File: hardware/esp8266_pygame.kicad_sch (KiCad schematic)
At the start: 27 parts, among them J1 Conn_01x12, J2 Conn_01x12, J3 Conn_01x03, J4 Conn_01x02, J5 Micro_SD_Card, J6 Conn_01x08, Q1 NPN, SW1 SW_Push, SW2 SW_Push, SW3 SW_Push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

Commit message: New PCB schematic ready
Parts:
- removed BZ1: Buzzer, symbol Device:Buzzer
- removed C1: 4u7, symbol Device:C
- removed D1: LED, symbol Device:LED
- removed J1, J2: Conn_01x12, symbol Connector_Generic:Conn_01x12
- removed J3: Conn_01x03, symbol Connector_Generic:Conn_01x03
- removed J4: Conn_01x02, symbol Connector_Generic:Conn_01x02
- removed J5: Micro_SD_Card, symbol Connector:Micro_SD_Card
- removed J6: Conn_01x08, symbol Connector_Generic:Conn_01x08
- removed Q1: NPN, symbol Simulation_SPICE:NPN
- removed R6: 142k, symbol Device:R
- removed R7: 200, symbol Device:R
- removed R8: 10k, symbol Device:R
- removed RN1: 9 x 10k, Resistor_THT:R_Array_SIP10, symbol Device:R_Network09
- removed RV?: 10k, symbol Device:R_Potentiometer
- removed SW1, SW2, SW3, SW4, SW5, SW6, SW7: SW_Push, symbol Switch:SW_Push
- removed SW8: SW_SPST, symbol Switch:SW_SPST
- removed U1: PCF8574, symbol Interface_Expansion:PCF8574
- added J1: Conn_02x02_Odd_Even, symbol Connector_Generic:Conn_02x02_Odd_Even
- added R2: 50k, symbol Device:R
- added R4: 10k, symbol Device:R
- added U1: ESP-07, RF_Module:ESP-07, symbol RF_Module:ESP-07
- R1: value 1k -> 0
- R3: value 100 -> 50k
- R5: value 220k -> 10k
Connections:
- net LED is gone; now on net LCD_CE: R3.1
- net +3.3V: now also R3.2, R5.2, R4.2, U1.8 (VCC)
- net BUZZER: now also R2.2, U1.6 (GPIO12)
- net GND: now also R2.1, U1.9 (GND)
- net LCD_CE: now also J1.4 (Pin_4), U1.12 (GPIO0)
- net LCD_DC: now also U1.11 (GPIO2)
- net LCD_RST: now also R1.2
- net MOSI: now also U1.7 (GPIO13)
- net RXD: now also J1.2 (Pin_2), U1.15 (GPIO3/RXD)
- net SCK: now also U1.5 (GPIO14)
- net SCL: now also U1.14 (GPIO5)
- net SDA: now also U1.13 (GPIO4)
- net TXD: now also J1.1 (Pin_1), U1.16 (GPIO1/TXD)
- net Ubatt: now also U1.2 (ADC); no longer R5.2
- net at R1.1: now also U1.4 (GPIO16)
- net +BATT renamed ~{RST}
- net ~{RST}: now also J1.3 (Pin_3), U1.1 (~{RST})
- new net BACKLIGHT_PWM: U1.10 (GPIO15)
- new net CHIP_EN: R4.1, U1.3 (EN)
- no-connect marks 9 -> 0
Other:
- added sheet Human Machine Interface Section (hmi.kicad_sch)
- added sheet Power section (power_section.kicad_sch)
- note removed: "3V3"
- note removed: "5V"
- note removed: "A0"
- note removed: "Battery"
- note removed: "Board Batt Conn"
- note removed: "CTS"
- note removed: "DTR"
- note removed: "EN"
- note removed: "GND"
- note removed: "GPIO0"
- note removed: "GPIO1"
- note removed: "GPIO12"
- note removed: "GPIO13"
- note removed: "GPIO14"
- note removed: "GPIO15"
- note removed: "GPIO16"
- note removed: "GPIO2"
- note removed: "GPIO3"
- note removed: "GPIO4"
- note removed: "GPIO5"
- note removed: "RST"

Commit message: Second revision of schematic
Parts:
- removed R4: 10k, symbol Device:R
- added R5, R6: 4k7, Resistor_SMD:R_0603_1608Metric, symbol Device:R
- J1: footprint (none) -> Connector_PinHeader_2.54mm:PinHeader_2x02_P2.54mm_Vertical
- R1, R2, R3: footprint (none) -> Resistor_SMD:R_0603_1608Metric
- R4: renamed from R5; footprint (none) -> Resistor_SMD:R_0603_1608Metric
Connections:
- net +3.3V: now also R5.2, R6.2
- net SCL: now also R6.1
- net SDA: now also R5.1
- net CHIP_EN: no longer names the net of U1.3 (EN)
- no-connect marks 0 -> 1
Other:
- sheet Human Machine Interface Section ports: added BACKLIGHT_PWM, BUZZER, LCD_CE, LCD_DC, LCD_RST, MOSI, POWER_EN, SCK, SCL, SDA; removed none
- sheet Power section ports: added POWER_EN, Ubatt; removed none
- moved on the sheet: R4

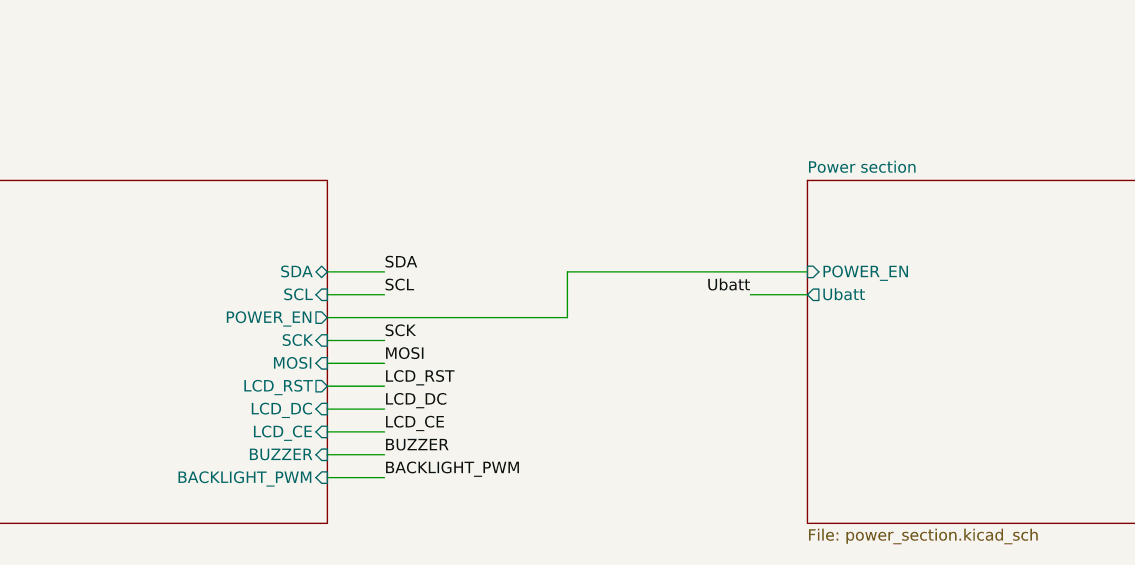
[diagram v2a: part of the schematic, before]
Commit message: Fixed power enable bypass
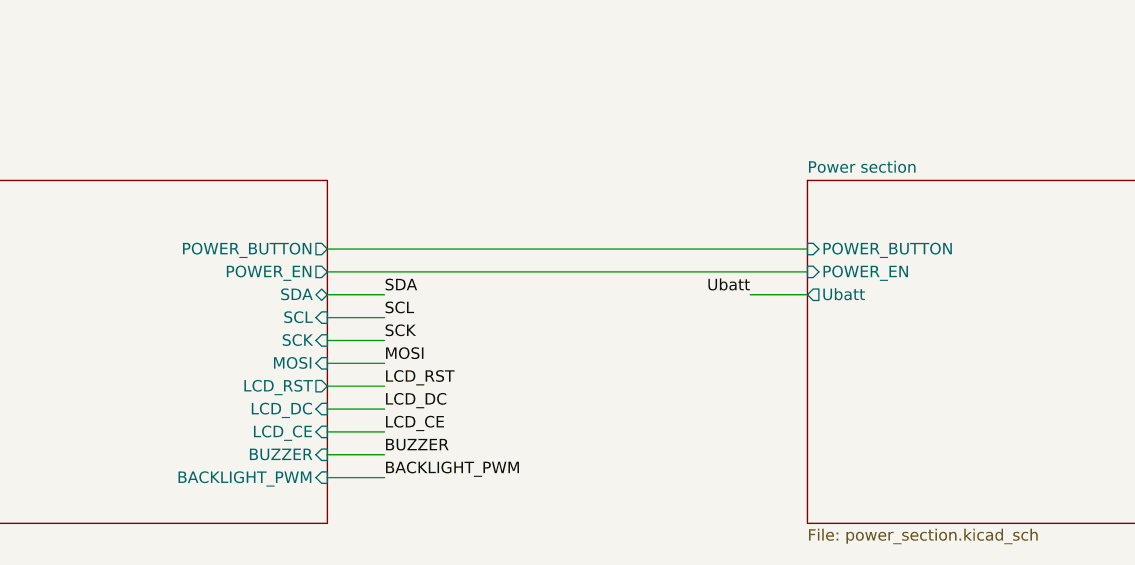
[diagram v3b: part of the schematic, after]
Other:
- sheet Human Machine Interface Section ports: added POWER_BUTTON; removed none
- sheet Power section ports: added POWER_BUTTON; removed none
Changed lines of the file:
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@@
 	(wire
 		(pts
-			(xy 146.05 130.81) (xy 146.05 125.73)
+			(xy 119.38 130.81) (xy 125.73 130.81)
+		)
+		(stroke
+			(width 0)
+			(type default)
+		)
+	)
+	(wire
+		(pts
+			(xy 119.38 123.19) (xy 172.72 123.19)
+		)
+		(stroke
+			(width 0)
+			(type default)
+		)
+	)
+	(wire
+		(pts
+			(xy 85.09 52.07) (xy 93.98 52.07)
+		)
+		(stroke
+			(width 0)
+			(type default)
+		)
+	)
+	(wire
+		(pts
+			(xy 85.09 57.15) (xy 93.98 57.15)
+		)
+		(stroke
+			(width 0)
+			(type default)
+		)
+	)
+	(wire
+		(pts
+			(xy 149.86 52.07) (xy 149.86 58.42)
+		)
+		(stroke
+			(width 0)
+			(type default)
+		)
+	)
+	(wire
+		(pts
+			(xy 46.99 41.91) (xy 54.61 41.91)
+		)
+		(stroke
+			(width 0)
+			(type default)
+		)
+	)
+	(wire
+		(pts
+			(xy 219.71 48.26) (xy 224.79 48.26)
+		)
+		(stroke
+			(width 0)
+			(type default)
+		)
+	)
+	(wire
+		(pts
+			(xy 69.85 74.93) (xy 69.85 82.55)
+		)
+		(stroke
+			(width 0)
+			(type default)
+		)
+	)
+	(wire
+		(pts
+			(xy 119.38 146.05) (xy 125.73 146.05)
 		)
 		(stroke
@@
 	(wire
 		(pts
-			(xy 85.09 52.07) (xy 93.98 52.07)
-		)
-		(stroke
-			(width 0)
-			(type default)
-		)
-	)
-	(wire
-		(pts
-			(xy 85.09 57.15) (xy 93.98 57.15)
-		)
-		(stroke
-			(width 0)
-			(type default)
-		)
-	)
-	(wire
-		(pts
-			(xy 149.86 52.07) (xy 149.86 58.42)
-		)
-		(stroke
-			(width 0)
-			(type default)
-		)
-	)
-	(wire
-		(pts
-			(xy 46.99 41.91) (xy 54.61 41.91)
-		)
-		(stroke
-			(width 0)
-			(type default)
-		)
-	)
-	(wire
-		(pts
-			(xy 146.05 125.73) (xy 172.72 125.73)
-		)
-		(stroke
-			(width 0)
-			(type default)
-		)
-	)
-	(wire
-		(pts
-			(xy 219.71 48.26) (xy 224.79 48.26)
-		)
-		(stroke
-			(width 0)
-			(type default)
-		)
-	)
-	(wire
-		(pts
-			(xy 69.85 74.93) (xy 69.85 82.55)
-		)
-		(stroke
-			(width 0)
-			(type default)
-		)
-	)
-	(wire
-		(pts
-			(xy 119.38 146.05) (xy 125.73 146.05)
-		)
-		(stroke
-			(width 0)
-			(type default)
-		)
-	)
-	(wire
-		(pts
-			(xy 119.38 125.73) (xy 125.73 125.73)
-		)
-		(stroke
-			(width 0)
-			(type default)
-		)
-	)
-	(wire
-		(pts
 			(xy 85.09 46.99) (xy 93.98 46.99)
 		)
@@
 	(wire
 		(pts
-			(xy 119.38 130.81) (xy 146.05 130.81)
+			(xy 119.38 125.73) (xy 172.72 125.73)
 		)
 		(stroke
@@
 	)
 	(label "SDA"
-		(at 125.73 125.73 0)
+		(at 125.73 128.27 0)
 		(effects
 			(font
@@
 	)
 	(label "SCL"
-		(at 125.73 128.27 0)
+		(at 125.73 130.81 0)
 		(effects
 			(font
@@
 		)
 		(pin "POWER_EN" output
-			(at 119.38 130.81 0)
+			(at 119.38 125.73 0)
 			(effects
 				(font
@@
 		)
 		(pin "SCL" input
+			(at 119.38 130.81 0)
+			(effects
+				(font
+					(size 1.27 1.27)
+				)
+				(justify right)
+			)
+		)
+		(pin "SDA" bidirectional
 			(at 119.38 128.27 0)
 			(effects
@@
 			)
 		)
-		(pin "SDA" bidirectional
-			(at 119.38 125.73 0)
+		(pin "POWER_BUTTON" output
+			(at 119.38 123.19 0)
 			(effects
 				(font
@@
 			(effects
 				(font
+					(size 1.27 1.27)
+				)
+				(justify left)
+			)
+		)
+		(pin "POWER_BUTTON" input
+			(at 172.72 123.19 180)
+			(effects
+				(font
